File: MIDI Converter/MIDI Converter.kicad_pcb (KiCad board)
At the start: 2 copper layers, 62.6 x 59.2 mm, 4 parts, among them J12 Conn_01x03_Socket, J13 DB25_Plug_MountingHoles, J2 Screw_Terminal_01x02, U1 Pico

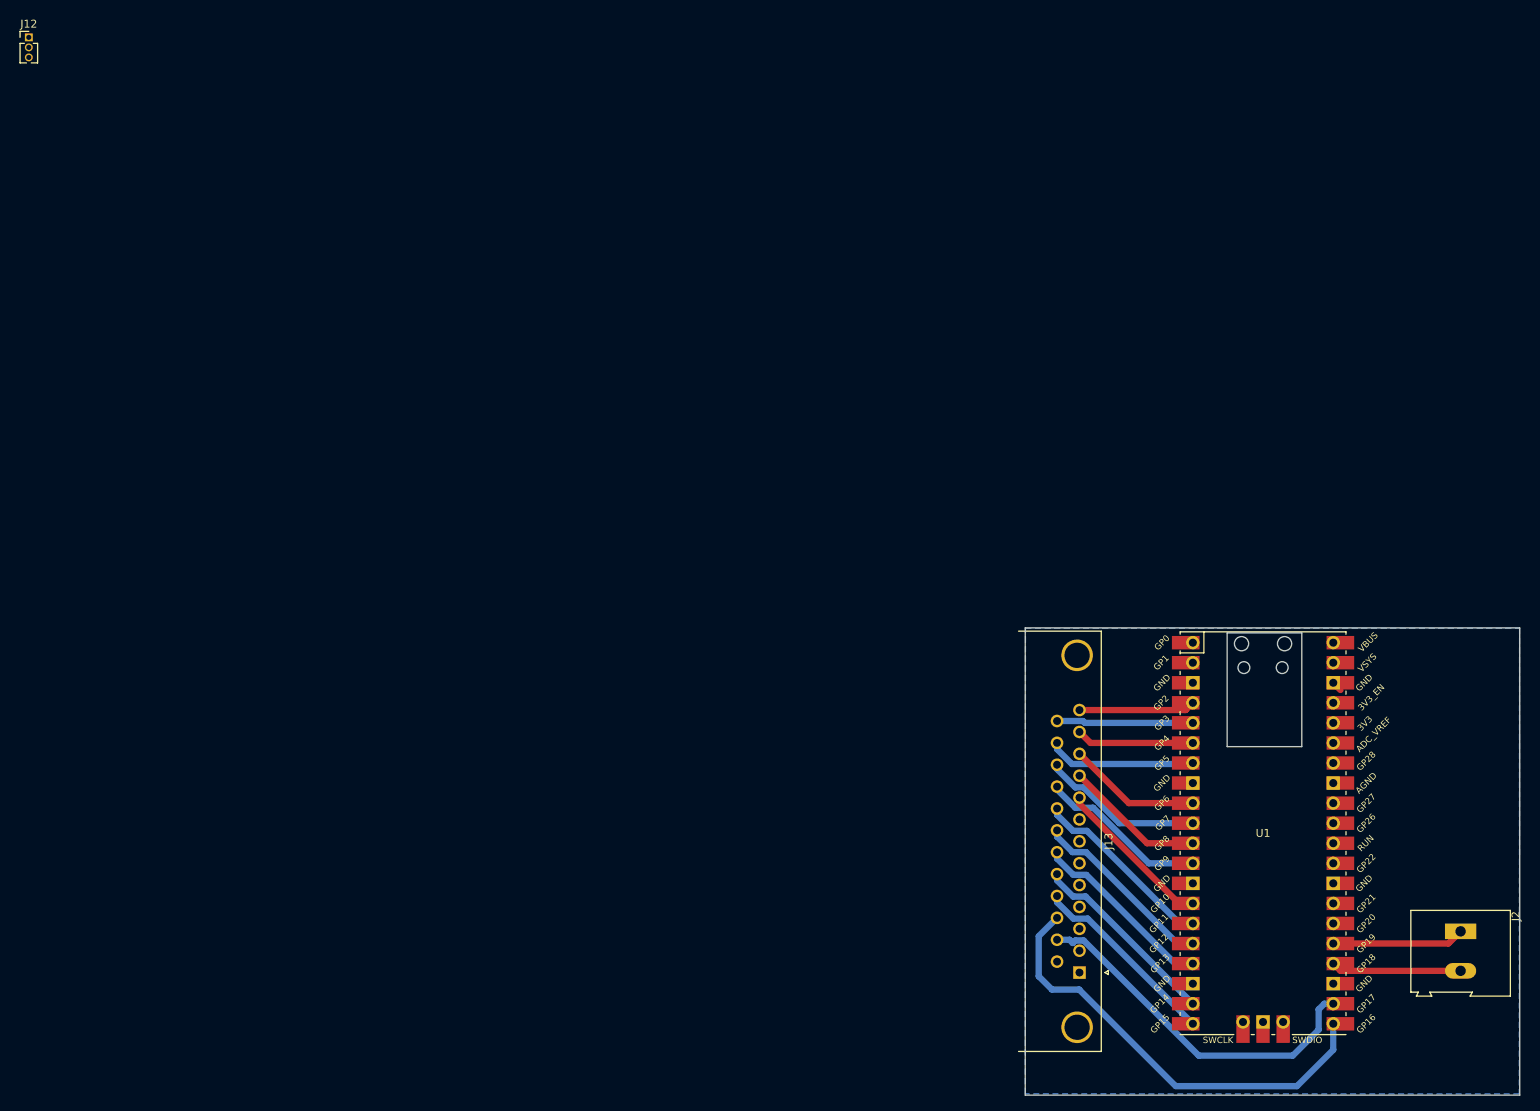
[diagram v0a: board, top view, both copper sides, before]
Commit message: Fixed socket size an refilled ground plane
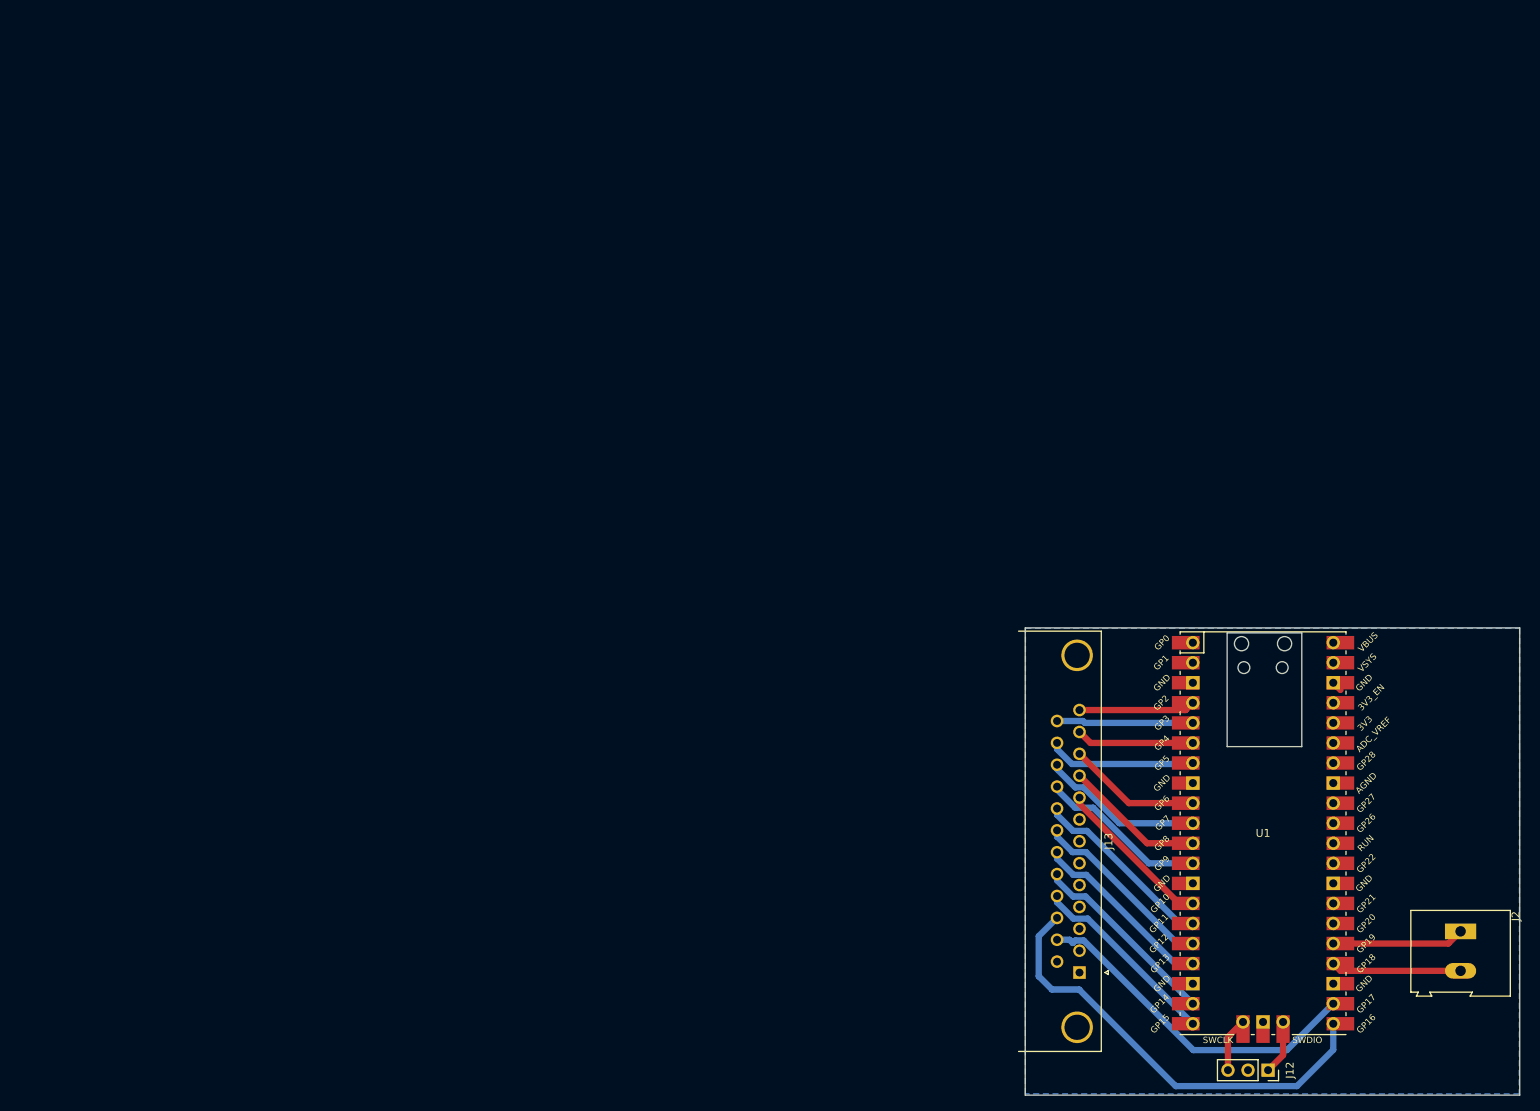
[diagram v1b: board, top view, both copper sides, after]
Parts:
- J12: footprint Connector_PinHeader_1.27mm:PinHeader_1x03_P1.27mm_Vertical -> Connector_PinSocket_2.54mm:PinSocket_1x03_P2.54mm_Vertical
- moved J12 204.3 mm to (158.5, 132.0), turned to -90 degrees
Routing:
- net Net-(J12-Pin_3): track 0.00 -> 6.89 mm
- net Net-(J12-Pin_1): track 0.00 -> 6.89 mm
- net Net-(J13-P15): track 45.5 -> 43.5 mm
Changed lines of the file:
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@@
     )
   )
-  (footprint "Connector_PinHeader_1.27mm:PinHeader_1x03_P1.27mm_Vertical" (layer "F.Cu")
-    (at 1.575 1.175)
-    (descr "Through hole straight pin header, 1x03, 1.27mm pitch, single row")
-    (tags "Through hole pin header THT 1x03 1.27mm single row")
+  (footprint "Connector_PinSocket_2.54mm:PinSocket_1x03_P2.54mm_Vertical" (layer "F.Cu")
+    (at 158.5 131.96 -90)
+    (descr "Through hole straight socket strip, 1x03, 2.54mm pitch, single row (from Kicad 4.0.7), script generated")
+    (tags "Through hole socket strip THT 1x03 2.54mm single row")
     (property "Sheetfile" "MIDI Converter.kicad_sch")
     (property "Sheetname" "")
@@
     (property "ki_keywords" "connector")
     (attr through_hole)
-    (fp_text reference "J12" (at 0 -1.695) (layer "F.SilkS")
-        (effects (font (size 1 1) (thickness 0.15)))
-    )
-    (fp_text value "Conn_01x03_Socket" (at 0 4.235) (layer "F.Fab")
-        (effects (font (size 1 1) (thickness 0.15)))
-    )
-    (fp_text user "${REFERENCE}" (at 0 1.27 90) (layer "F.Fab")
-        (effects (font (size 1 1) (thickness 0.15)))
-    )
-    (fp_line (start -1.11 -0.76) (end 0 -0.76)
-      (stroke (width 0.12) (type solid)) (layer "F.SilkS"))
-    (fp_line (start -1.11 0) (end -1.11 -0.76)
-      (stroke (width 0.12) (type solid)) (layer "F.SilkS"))
-    (fp_line (start -1.11 0.76) (end -1.11 3.235)
-      (stroke (width 0.12) (type solid)) (layer "F.SilkS"))
-    (fp_line (start -1.11 0.76) (end -0.563471 0.76)
-      (stroke (width 0.12) (type solid)) (layer "F.SilkS"))
-    (fp_line (start -1.11 3.235) (end -0.30753 3.235)
-      (stroke (width 0.12) (type solid)) (layer "F.SilkS"))
-    (fp_line (start 0.30753 3.235) (end 1.11 3.235)
-      (stroke (width 0.12) (type solid)) (layer "F.SilkS"))
-    (fp_line (start 0.563471 0.76) (end 1.11 0.76)
-      (stroke (width 0.12) (type solid)) (layer "F.SilkS"))
-    (fp_line (start 1.11 0.76) (end 1.11 3.235)
-      (stroke (width 0.12) (type solid)) (layer "F.SilkS"))
-    (fp_line (start -1.55 -1.15) (end -1.55 3.7)
+    (fp_text reference "J12" (at 0 -2.77 -90) (layer "F.SilkS")
+        (effects (font (size 1 1) (thickness 0.15)))
+    )
+    (fp_text value "Conn_01x03_Socket" (at 0 7.85 -90) (layer "F.Fab")
+        (effects (font (size 1 1) (thickness 0.15)))
+    )
+    (fp_text user "${REFERENCE}" (at 0 2.54) (layer "F.Fab")
+        (effects (font (size 1 1) (thickness 0.15)))
+    )
+    (fp_line (start -1.33 1.27) (end -1.33 6.41)
+      (stroke (width 0.12) (type solid)) (layer "F.SilkS"))
+    (fp_line (start -1.33 1.27) (end 1.33 1.27)
+      (stroke (width 0.12) (type solid)) (layer "F.SilkS"))
+    (fp_line (start -1.33 6.41) (end 1.33 6.41)
+      (stroke (width 0.12) (type solid)) (layer "F.SilkS"))
+    (fp_line (start 0 -1.33) (end 1.33 -1.33)
+      (stroke (width 0.12) (type solid)) (layer "F.SilkS"))
+    (fp_line (start 1.33 -1.33) (end 1.33 0)
+      (stroke (width 0.12) (type solid)) (layer "F.SilkS"))
+    (fp_line (start 1.33 1.27) (end 1.33 6.41)
+      (stroke (width 0.12) (type solid)) (layer "F.SilkS"))
+    (fp_line (start -1.8 -1.8) (end 1.75 -1.8)
       (stroke (width 0.05) (type solid)) (layer "F.CrtYd"))
-    (fp_line (start -1.55 3.7) (end 1.55 3.7)
+    (fp_line (start -1.8 6.85) (end -1.8 -1.8)
       (stroke (width 0.05) (type solid)) (layer "F.CrtYd"))
-    (fp_line (start 1.55 -1.15) (end -1.55 -1.15)
+    (fp_line (start 1.75 -1.8) (end 1.75 6.85)
       (stroke (width 0.05) (type solid)) (layer "F.CrtYd"))
-    (fp_line (start 1.55 3.7) (end 1.55 -1.15)
+    (fp_line (start 1.75 6.85) (end -1.8 6.85)
       (stroke (width 0.05) (type solid)) (layer "F.CrtYd"))
-    (fp_line (start -1.05 -0.11) (end -0.525 -0.635)
+    (fp_line (start -1.27 -1.27) (end 0.635 -1.27)
       (stroke (width 0.1) (type solid)) (layer "F.Fab"))
-    (fp_line (start -1.05 3.175) (end -1.05 -0.11)
+    (fp_line (start -1.27 6.35) (end -1.27 -1.27)
       (stroke (width 0.1) (type solid)) (layer "F.Fab"))
-    (fp_line (start -0.525 -0.635) (end 1.05 -0.635)
+    (fp_line (start 0.635 -1.27) (end 1.27 -0.635)
       (stroke (width 0.1) (type solid)) (layer "F.Fab"))
-    (fp_line (start 1.05 -0.635) (end 1.05 3.175)
+    (fp_line (start 1.27 -0.635) (end 1.27 6.35)
       (stroke (width 0.1) (type solid)) (layer "F.Fab"))
-    (fp_line (start 1.05 3.175) (end -1.05 3.175)
+    (fp_line (start 1.27 6.35) (end -1.27 6.35)
       (stroke (width 0.1) (type solid)) (layer "F.Fab"))
-    (pad "1" thru_hole rect (at 0 0) (size 1 1) (drill 0.65) (layers "*.Cu" "*.Mask")
+    (pad "1" thru_hole rect (at 0 0 270) (size 1.7 1.7) (drill 1) (layers "*.Cu" "*.Mask")
       (net 19 "Net-(J12-Pin_1)") (pinfunction "Pin_1") (pintype "passive"))
-    (pad "2" thru_hole oval (at 0 1.27) (size 1 1) (drill 0.65) (layers "*.Cu" "*.Mask")
+    (pad "2" thru_hole oval (at 0 2.54 270) (size 1.7 1.7) (drill 1) (layers "*.Cu" "*.Mask")
       (net 3 "GND") (pinfunction "Pin_2") (pintype "passive"))
-    (pad "3" thru_hole oval (at 0 2.54) (size 1 1) (drill 0.65) (layers "*.Cu" "*.Mask")
+    (pad "3" thru_hole oval (at 0 5.08 270) (size 1.7 1.7) (drill 1) (layers "*.Cu" "*.Mask")
       (net 20 "Net-(J12-Pin_3)") (pinfunction "Pin_3") (pintype "passive"))
-    (model "${KICAD6_3DMODEL_DIR}/Connector_PinHeader_1.27mm.3dshapes/PinHeader_1x03_P1.27mm_Vertical.wrl"
+    (model "${KICAD6_3DMODEL_DIR}/Connector_PinSocket_2.54mm.3dshapes/PinSocket_1x03_P2.54mm_Vertical.wrl"
       (offset (xyz 0 0 0))
       (scale (xyz 1 1 1))
@@
   (segment (start 167.67 119.38) (end 166.755 118.465) (width 0.8) (layer "F.Cu") (net 2))
   (segment (start 182.88 119.38) (end 167.67 119.38) (width 0.8) (layer "F.Cu") (net 2))
+  (segment (start 160.405 130.055) (end 158.5 131.96) (width 0.8) (layer "F.Cu") (net 19))
+  (segment (start 160.405 125.855) (end 160.405 130.055) (width 0.8) (layer "F.Cu") (net 19))
+  (segment (start 153.42 127.76) (end 155.325 125.855) (width 0.8) (layer "F.Cu") (net 20))
+  (segment (start 153.42 131.96) (end 153.42 127.76) (width 0.8) (layer "F.Cu") (net 20))
   (segment (start 147.225 110.845) (end 148.975 110.845) (width 0.8) (layer "F.Cu") (net 29))
   (segment (start 134.62 98.24) (end 147.225 110.845) (width 0.8) (layer "F.Cu") (net 29))
@@
   (segment (start 134.62 86.36) (end 148.06 86.36) (width 0.8) (layer "F.Cu") (net 33))
   (segment (start 148.06 86.36) (end 148.975 85.445) (width 0.8) (layer "F.Cu") (net 33))
-  (segment (start 133.771389 115.861389) (end 133.355 115.445) (width 0.8) (layer "B.Cu") (net 35))
-  (segment (start 135.147222 115.54) (end 134.092778 115.54) (width 0.8) (layer "B.Cu") (net 35))
-  (segment (start 161.62 130.12) (end 149.727222 130.12) (width 0.8) (layer "B.Cu") (net 35))
-  (segment (start 165.625 123.545) (end 164.9 124.27) (width 0.8) (layer "B.Cu") (net 35))
-  (segment (start 149.727222 130.12) (end 135.147222 115.54) (width 0.8) (layer "B.Cu") (net 35))
+  (segment (start 134.085664 115.54) (end 133.767832 115.857832) (width 0.8) (layer "B.Cu") (net 35))
   (segment (start 133.355 115.445) (end 131.78 115.445) (width 0.8) (layer "B.Cu") (net 35))
-  (segment (start 164.9 124.27) (end 164.9 126.84) (width 0.8) (layer "B.Cu") (net 35))
-  (segment (start 166.755 123.545) (end 165.625 123.545) (width 0.8) (layer "B.Cu") (net 35))
-  (segment (start 134.092778 115.54) (end 133.771389 115.861389) (width 0.8) (layer "B.Cu") (net 35))
-  (segment (start 164.9 126.84) (end 161.62 130.12) (width 0.8) (layer "B.Cu") (net 35))
+  (segment (start 133.767832 115.857832) (end 133.355 115.445) (width 0.8) (layer "B.Cu") (net 35))
+  (segment (start 166.755 123.545) (end 160.88 129.42) (width 0.8) (layer "B.Cu") (net 35))
+  (segment (start 135.154336 115.54) (end 134.085664 115.54) (width 0.8) (layer "B.Cu") (net 35))
+  (segment (start 149.034336 129.42) (end 135.154336 115.54) (width 0.8) (layer "B.Cu") (net 35))
+  (segment (start 160.88 129.42) (end 149.034336 129.42) (width 0.8) (layer "B.Cu") (net 35))
   (segment (start 146.81 133.98) (end 162.16 133.98) (width 0.8) (layer "B.Cu") (net 36))
   (segment (start 129.46 120.08) (end 131.13 121.75) (width 0.8) (layer "B.Cu") (net 36))
